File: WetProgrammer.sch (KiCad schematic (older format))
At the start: 31 parts

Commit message: Added power flaggs to supress ERC errors
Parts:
- removed JP?: Jumper_3_Open, symbol Jumper:Jumper_3_Open
- added JP4: SolderJumper_3_Open, symbol Jumper:SolderJumper_3_Open
- JP1: renamed from JP?; symbol tmc:SolderJumper_3_Bridged12 -> WetProgrammer-rescue:SolderJumper_3_Bridged12-tmc
- JP5: renamed from JP?; symbol Jumper:Jumper_2_Open -> Jumper:SolderJumper_2_Open
- U1: renamed from U?; symbol tmc:ATmega32U4-AU -> WetProgrammer-rescue:ATmega32U4-AU-tmc
- Y1: renamed from Y?; symbol tmc:Crystal -> WetProgrammer-rescue:Crystal-tmc
- gave numbers to parts that had none: 24
- renumbered JDUT to JDUT1, JPROG to JPROG1
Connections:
- wire segments 113 -> 120

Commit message: Inital Layout
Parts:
- removed JP4: SolderJumper_3_Open, symbol Jumper:SolderJumper_3_Open
- added SW1: SW_SPDT, tmc:388Switch, symbol Switch:SW_SPDT
- added TP3: TestPoint, TestPoint:TestPoint_Pad_D1.5mm, symbol Connector:TestPoint
- C7, C8: footprint (none) -> Capacitor_SMD:C_0805_2012Metric
- F1: footprint (none) -> Fuse:Fuse_0805_2012Metric_Castellated
- J1: footprint tmc:usbMicro -> 388:usbMicro
- JP1: footprint Jumper:SolderJumper-3_P1.3mm_Bridged12_Pad1.0x1.5mm -> Jumper:SolderJumper-2_P1.3mm_Bridged_Pad1.0x1.5mm; symbol WetProgrammer-rescue:SolderJumper_3_Bridged12-tmc -> Jumper:SolderJumper_2_Bridged
- JP4: renamed from JP5; footprint (none) -> Connector_PinHeader_2.54mm:PinHeader_1x02_P2.54mm_Vertical; symbol Jumper:SolderJumper_2_Open -> Jumper:Jumper_2_Open
- JPROG1: footprint (none) -> Connector_PinHeader_1.27mm:PinHeader_2x05_P1.27mm_Vertical
- TP2: renamed from TP1; footprint TestPoint:TestPoint_Bridge_Pitch2.0mm_Drill0.7mm -> TestPoint:TestPoint_Pad_D1.5mm
- U2: footprint (none) -> Package_TO_SOT_SMD:SOT-223-3_TabPin2
- renumbered C2 to C1, C3 to C2, C1 to C3, JDUT1 to J2
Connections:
- wire segments 120 -> 124
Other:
- moved on the sheet: C3

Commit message: Changes as requested by Ben
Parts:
- removed JP4: Jumper_2_Open, Connector_PinHeader_2.54mm:PinHeader_1x02_P2.54mm_Vertical, symbol Jumper:Jumper_2_Open
- added FID1, FID2: Fiducial, Fiducial:Fiducial_1mm_Mask2mm, symbol Mechanical:Fiducial
- added H1, H2: MountingHole, MountingHole:MountingHole_3.2mm_M3, symbol Mechanical:MountingHole
- added J3: Conn_01x03_Male, Connector_PinHeader_2.54mm:PinHeader_1x03_P2.54mm_Vertical, symbol Connector:Conn_01x03_Male
- added R10, R11: 330, Resistor_SMD:R_0805_2012Metric, symbol Device:R
- added SW2: SW_SPDT, tmc:388Switch, symbol Switch:SW_SPDT
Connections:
- net GND: now also J3.3 (Pin_3)
- net VCC: now also SW2.1 (A)
- net VProg: now also SW2.2 (B)
- net at U1.20 (PD2): now also R10.2
- net at U1.21 (PD3): now also R11.2
- new net RXI: J3.2 (Pin_2), R11.1
- new net TXO: J3.1 (Pin_1), R10.1
- no-connect marks 16 -> 15
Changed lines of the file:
@@
 NoConn ~ 3400 2700
 NoConn ~ 3400 2800
-NoConn ~ 3400 2900
-NoConn ~ 3400 3000
 NoConn ~ 3400 3200
 NoConn ~ 3400 3300
@@
 P 3950 3550
 F 0 "#PWR013" H 3950 3400 50  0001 C CNN
-F 1 "VCC" H 3965 3723 50  0000 C CNN
+F 1 "VCC" H 3950 3700 50  0000 C CNN
 F 2 "" H 3950 3550 50  0001 C CNN
 F 3 "" H 3950 3550 50  0001 C CNN
@@
 	9500 1550 9500 1500
 $Comp
-L Jumper:Jumper_2_Open JP4
-U 1 1 6137D06D
-P 9200 1900
-F 0 "JP4" H 9200 1800 50  0000 C CNN
-F 1 "Jumper_2_Open" H 9200 1766 50  0001 C CNN
-F 2 "Connector_PinHeader_2.54mm:PinHeader_1x02_P2.54mm_Vertical" H 9200 1900 50  0001 C CNN
-F 3 "~" H 9200 1900 50  0001 C CNN
-	1    9200 1900
-	-1   0    0    1
-$EndComp
-$Comp
 L power:VCC #PWR021
 U 1 1 6137EE6D
-P 8950 1850
-F 0 "#PWR021" H 8950 1700 50  0001 C CNN
-F 1 "VCC" H 8965 2023 50  0000 C CNN
-F 2 "" H 8950 1850 50  0001 C CNN
-F 3 "" H 8950 1850 50  0001 C CNN
-	1    8950 1850
-	1    0    0    -1
-$EndComp
-Wire Wire Line
-	8950 1850 8950 1900
-Wire Wire Line
-	8950 1900 9000 1900
-Wire Wire Line
-	9400 1900 9650 1900
-Text Label 9650 1900 2    50   ~ 0
+P 8950 1900
+F 0 "#PWR021" H 8950 1750 50  0001 C CNN
+F 1 "VCC" H 8965 2073 50  0000 C CNN
+F 2 "" H 8950 1900 50  0001 C CNN
+F 3 "" H 8950 1900 50  0001 C CNN
+	1    8950 1900
+	1    0    0    -1
+$EndComp
+Wire Wire Line
+	8950 1900 8950 1950
+Wire Wire Line
+	8950 1950 9000 1950
+Wire Wire Line
+	9400 2050 9650 2050
+Text Label 9650 2050 2    50   ~ 0
 VProg
 Wire Wire Line
@@
 Text Notes 8900 700  0    50   ~ 0
 Voltage Select Jumper
-Text Notes 8950 2150 0    50   ~ 0
+Text Notes 8950 2400 0    50   ~ 0
 Programer Provides\nPower Select
 Text Notes 8050 850  0    50   ~ 0
@@
 Wire Wire Line
 	3800 2200 3800 2050
+$Comp
+L Mechanical:Fiducial FID2
+U 1 1 61492763
+P 650 7400
+F 0 "FID2" H 735 7446 50  0000 L CNN
+F 1 "Fiducial" H 735 7355 50  0000 L CNN
+F 2 "Fiducial:Fiducial_1mm_Mask2mm" H 650 7400 50  0001 C CNN
+F 3 "~" H 650 7400 50  0001 C CNN
+	1    650  7400
+	1    0    0    -1
+$EndComp
+$Comp
+L Mechanical:Fiducial FID1
+U 1 1 61492FAD
+P 650 7200
+F 0 "FID1" H 735 7246 50  0000 L CNN
+F 1 "Fiducial" H 735 7155 50  0000 L CNN
+F 2 "Fiducial:Fiducial_1mm_Mask2mm" H 650 7200 50  0001 C CNN
+F 3 "~" H 650 7200 50  0001 C CNN
+	1    650  7200
+	1    0    0    -1
+$EndComp
+$Comp
+L Mechanical:MountingHole H1
+U 1 1 61497033
+P 650 7600
+F 0 "H1" H 750 7646 50  0000 L CNN
+F 1 "MountingHole" H 750 7555 50  0000 L CNN
+F 2 "MountingHole:MountingHole_3.2mm_M3" H 650 7600 50  0001 C CNN
+F 3 "~" H 650 7600 50  0001 C CNN
+	1    650  7600
+	1    0    0    -1
+$EndComp
+$Comp
+L Mechanical:MountingHole H2
+U 1 1 6149BCA9
+P 650 7800
+F 0 "H2" H 750 7846 50  0000 L CNN
+F 1 "MountingHole" H 750 7755 50  0000 L CNN
+F 2 "MountingHole:MountingHole_3.2mm_M3" H 650 7800 50  0001 C CNN
+F 3 "~" H 650 7800 50  0001 C CNN
+	1    650  7800
+	1    0    0    -1
+$EndComp
+$Comp
+L Switch:SW_SPDT SW2
+U 1 1 614A9941
+P 9200 2050
+F 0 "SW2" H 9100 2150 50  0000 R CNN
+F 1 "SW_SPDT" V 9245 1862 50  0001 R CNN
+F 2 "tmc:388Switch" H 9200 2050 50  0001 C CNN
+F 3 "~" H 9200 2050 50  0001 C CNN
+	1    9200 2050
+	-1   0    0    -1
+$EndComp
+NoConn ~ 9000 2150
+$Comp
+L Device:R R?
+U 1 1 614D3179
+P 3600 2900
+AR Path="/612E47B1/614D3179" Ref="R?"  Part="1"
+AR Path="/614D3179" Ref="R10"  Part="1"
+F 0 "R10" V 3550 3100 50  0000 C CNN
+F 1 "330" V 3600 2900 50  0000 C CNN
+F 2 "Resistor_SMD:R_0805_2012Metric" V 3530 2900 50  0001 C CNN
+F 3 "~" H 3600 2900 50  0001 C CNN
+	1    3600 2900
+	0    1    1    0
+$EndComp
+Wire Wire Line
+	3450 2900 3400 2900
+$Comp
+L Device:R R?
+U 1 1 614D6E84
+P 3600 3000
+AR Path="/612E47B1/614D6E84" Ref="R?"  Part="1"
+AR Path="/614D6E84" Ref="R11"  Part="1"
+F 0 "R11" V 3550 3200 50  0000 C CNN
+F 1 "330" V 3600 3000 50  0000 C CNN
+F 2 "Resistor_SMD:R_0805_2012Metric" V 3530 3000 50  0001 C CNN
+F 3 "~" H 3600 3000 50  0001 C CNN
+	1    3600 3000
+	0    1    1    0
+$EndComp
+Wire Wire Line
+	3450 3000 3400 3000
+Text Label 4050 3000 2    50   ~ 0
+RXI
+Text Label 4050 2900 2    50   ~ 0
+TXO
+$Comp
+L Connector:Conn_01x03_Male J3
+U 1 1 614ECA92
+P 4300 3000
+F 0 "J3" H 4272 2978 50  0000 R CNN
+F 1 "Conn_01x03_Male" H 4272 2933 50  0001 R CNN
+F 2 "Connector_PinHeader_2.54mm:PinHeader_1x03_P2.54mm_Vertical" H 4300 3000 50  0001 C CNN
+F 3 "~" H 4300 3000 50  0001 C CNN
+	1    4300 3000
+	-1   0    0    -1
+$EndComp
+Wire Wire Line
+	3750 2900 4100 2900
+Wire Wire Line
+	3750 3000 4100 3000
+$Comp
+L power:GND #PWR?
+U 1 1 614F6BB5
+P 4050 3150
+AR Path="/612E47B1/614F6BB5" Ref="#PWR?"  Part="1"
+AR Path="/614F6BB5" Ref="#PWR0101"  Part="1"
+F 0 "#PWR0101" H 4050 2900 50  0001 C CNN
+F 1 "GND" H 4050 3000 50  0000 C CNN
+F 2 "" H 4050 3150 50  0001 C CNN
+F 3 "" H 4050 3150 50  0001 C CNN
+	1    4050 3150
+	1    0    0    -1
+$EndComp
+Wire Wire Line
+	4050 3150 4050 3100
+Wire Wire Line
+	4050 3100 4100 3100
 $EndSCHEMATC

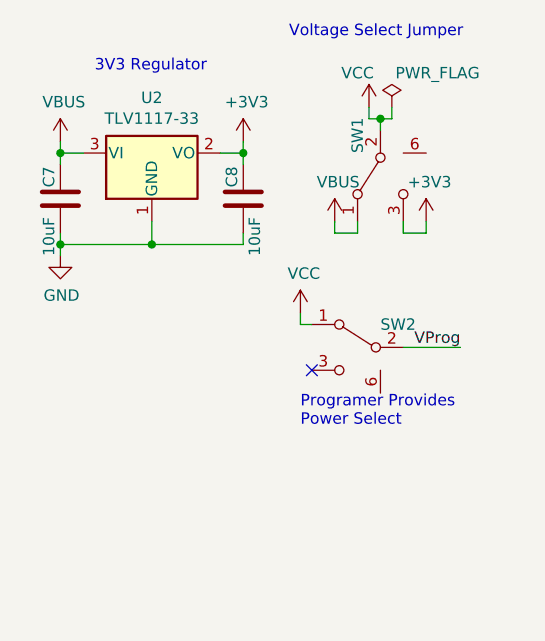
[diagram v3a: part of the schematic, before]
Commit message: Connected swtich sheilding to gnd
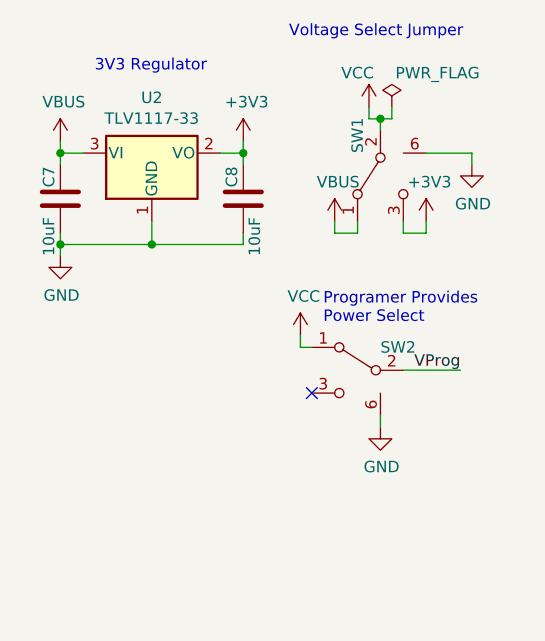
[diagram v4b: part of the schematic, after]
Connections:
- net GND: now also SW1.6 (sheild), SW2.6 (sheild)
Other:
- moved on the sheet: SW2
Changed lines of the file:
@@
 Connection ~ 8300 1600
-$Comp
-L power:VBUS #PWR?
-U 1 1 6136D7E0
-P 9100 1500
-AR Path="/612E47B1/6136D7E0" Ref="#PWR?"  Part="1"
-AR Path="/6136D7E0" Ref="#PWR022"  Part="1"
-F 0 "#PWR022" H 9100 1350 50  0001 C CNN
-F 1 "VBUS" H 9115 1673 50  0000 C CNN
-F 2 "" H 9100 1500 50  0001 C CNN
-F 3 "" H 9100 1500 50  0001 C CNN
-	1    9100 1500
-	1    0    0    -1
-$EndComp
-$Comp
-L power:+3V3 #PWR?
-U 1 1 613709A8
-P 9500 1500
-AR Path="/612E47B1/613709A8" Ref="#PWR?"  Part="1"
-AR Path="/613709A8" Ref="#PWR024"  Part="1"
-F 0 "#PWR024" H 9500 1350 50  0001 C CNN
-F 1 "+3V3" H 9515 1673 50  0000 C CNN
-F 2 "" H 9500 1500 50  0001 C CNN
-F 3 "" H 9500 1500 50  0001 C CNN
-	1    9500 1500
-	1    0    0    -1
-$EndComp
-$Comp
-L power:VCC #PWR023
-U 1 1 61370E3F
-P 9250 1000
-F 0 "#PWR023" H 9250 850 50  0001 C CNN
-F 1 "VCC" H 9200 1150 50  0000 C CNN
-F 2 "" H 9250 1000 50  0001 C CNN
-F 3 "" H 9250 1000 50  0001 C CNN
-	1    9250 1000
-	1    0    0    -1
-$EndComp
-Wire Wire Line
-	9100 1550 9100 1500
-Wire Wire Line
-	9500 1550 9500 1500
 $Comp
 L power:VCC #PWR021
 U 1 1 6137EE6D
-P 8950 1900
-F 0 "#PWR021" H 8950 1750 50  0001 C CNN
-F 1 "VCC" H 8965 2073 50  0000 C CNN
-F 2 "" H 8950 1900 50  0001 C CNN
-F 3 "" H 8950 1900 50  0001 C CNN
-	1    8950 1900
-	1    0    0    -1
-$EndComp
-Wire Wire Line
-	8950 1900 8950 1950
-Wire Wire Line
-	8950 1950 9000 1950
-Wire Wire Line
-	9400 2050 9650 2050
-Text Label 9650 2050 2    50   ~ 0
+P 8950 2000
+F 0 "#PWR021" H 8950 1850 50  0001 C CNN
+F 1 "VCC" H 8965 2173 50  0000 C CNN
+F 2 "" H 8950 2000 50  0001 C CNN
+F 3 "" H 8950 2000 50  0001 C CNN
+	1    8950 2000
+	1    0    0    -1
+$EndComp
+Wire Wire Line
+	8950 2000 8950 2050
+Wire Wire Line
+	8950 2050 9000 2050
+Wire Wire Line
+	9400 2150 9650 2150
+Text Label 9650 2150 2    50   ~ 0
 VProg
 Wire Wire Line
@@
 Text Notes 8900 700  0    50   ~ 0
 Voltage Select Jumper
-Text Notes 8950 2400 0    50   ~ 0
+Text Notes 9050 1950 0    50   ~ 0
 Programer Provides\nPower Select
 Text Notes 8050 850  0    50   ~ 0
@@
 	1400 2650 1400 2600
 Connection ~ 1400 2650
-$Comp
-L power:PWR_FLAG #FLG02
-U 1 1 61448067
-P 9350 1000
-F 0 "#FLG02" H 9350 1075 50  0001 C CNN
-F 1 "PWR_FLAG" H 9550 1150 50  0000 C CNN
-F 2 "" H 9350 1000 50  0001 C CNN
-F 3 "~" H 9350 1000 50  0001 C CNN
-	1    9350 1000
-	1    0    0    -1
-$EndComp
-Wire Wire Line
-	9350 1000 9350 1050
-Wire Wire Line
-	9350 1050 9300 1050
-Wire Wire Line
-	9250 1050 9250 1000
-Wire Wire Line
-	9300 1100 9300 1050
-Connection ~ 9300 1050
-Wire Wire Line
-	9300 1050 9250 1050
 $Comp
 L Jumper:SolderJumper_2_Bridged JP?
@@
 Wire Wire Line
 	3800 2050 3800 2000
-$Comp
-L Switch:SW_SPDT SW1
-U 1 1 61486C4E
-P 9300 1300
-F 0 "SW1" H 9200 1400 50  0000 R CNN
-F 1 "SW_SPDT" V 9345 1112 50  0001 R CNN
-F 2 "tmc:388Switch" H 9300 1300 50  0001 C CNN
-F 3 "~" H 9300 1300 50  0001 C CNN
-	1    9300 1300
-	0    -1   1    0
-$EndComp
-Wire Wire Line
-	9200 1550 9200 1500
 Wire Wire Line
 	9100 1550 9200 1550
-Wire Wire Line
-	9400 1550 9400 1500
 Wire Wire Line
 	9400 1550 9500 1550
@@
 L Switch:SW_SPDT SW2
 U 1 1 614A9941
-P 9200 2050
-F 0 "SW2" H 9100 2150 50  0000 R CNN
-F 1 "SW_SPDT" V 9245 1862 50  0001 R CNN
-F 2 "tmc:388Switch" H 9200 2050 50  0001 C CNN
-F 3 "~" H 9200 2050 50  0001 C CNN
-	1    9200 2050
+P 9200 2150
+F 0 "SW2" H 9100 2250 50  0000 R CNN
+F 1 "SW_SPDT" V 9245 1962 50  0001 R CNN
+F 2 "tmc:388Switch" H 9200 2150 50  0001 C CNN
+F 3 "~" H 9200 2150 50  0001 C CNN
+	1    9200 2150
 	-1   0    0    -1
 $EndComp
-NoConn ~ 9000 2150
+NoConn ~ 9000 2250
 $Comp
 L Device:R R?
@@
 Wire Wire Line
 	4050 3100 4100 3100
+$Comp
+L power:GND #PWR?
+U 1 1 614B5DDC
+P 9700 1250
+F 0 "#PWR?" H 9700 1000 50  0001 C CNN
+F 1 "GND" H 9705 1077 50  0000 C CNN
+F 2 "" H 9700 1250 50  0001 C CNN
+F 3 "" H 9700 1250 50  0001 C CNN
+	1    9700 1250
+	1    0    0    -1
+$EndComp
+Wire Wire Line
+	9400 1550 9400 1500
+Wire Wire Line
+	9200 1550 9200 1500
+$Comp
+L Switch:SW_SPDT SW1
+U 1 1 61486C4E
+P 9300 1300
+F 0 "SW1" H 9200 1400 50  0000 R CNN
+F 1 "SW_SPDT" V 9345 1112 50  0001 R CNN
+F 2 "tmc:388Switch" H 9300 1300 50  0001 C CNN
+F 3 "~" H 9300 1300 50  0001 C CNN
+	1    9300 1300
+	0    -1   1    0
+$EndComp
+Wire Wire Line
+	9300 1050 9250 1050
+Connection ~ 9300 1050
+Wire Wire Line
+	9300 1100 9300 1050
+Wire Wire Line
+	9250 1050 9250 1000
+Wire Wire Line
+	9350 1050 9300 1050
+Wire Wire Line
+	9350 1000 9350 1050
+$Comp
+L power:PWR_FLAG #FLG02
+U 1 1 61448067
+P 9350 1000
+F 0 "#FLG02" H 9350 1075 50  0001 C CNN
+F 1 "PWR_FLAG" H 9550 1150 50  0000 C CNN
+F 2 "" H 9350 1000 50  0001 C CNN
+F 3 "~" H 9350 1000 50  0001 C CNN
+	1    9350 1000
+	1    0    0    -1
+$EndComp
+Wire Wire Line
+	9500 1550 9500 1500
+Wire Wire Line
+	9100 1550 9100 1500
+$Comp
+L power:VCC #PWR023
+U 1 1 61370E3F
+P 9250 1000
+F 0 "#PWR023" H 9250 850 50  0001 C CNN
+F 1 "VCC" H 9200 1150 50  0000 C CNN
+F 2 "" H 9250 1000 50  0001 C CNN
+F 3 "" H 9250 1000 50  0001 C CNN
+	1    9250 1000
+	1    0    0    -1
+$EndComp
+$Comp
+L power:+3V3 #PWR?
+U 1 1 613709A8
+P 9500 1500
+AR Path="/612E47B1/613709A8" Ref="#PWR?"  Part="1"
+AR Path="/613709A8" Ref="#PWR024"  Part="1"
+F 0 "#PWR024" H 9500 1350 50  0001 C CNN
+F 1 "+3V3" H 9515 1673 50  0000 C CNN
+F 2 "" H 9500 1500 50  0001 C CNN
+F 3 "" H 9500 1500 50  0001 C CNN
+	1    9500 1500
+	1    0    0    -1
+$EndComp
+$Comp
+L power:VBUS #PWR?
+U 1 1 6136D7E0
+P 9100 1500
+AR Path="/612E47B1/6136D7E0" Ref="#PWR?"  Part="1"
+AR Path="/6136D7E0" Ref="#PWR022"  Part="1"
+F 0 "#PWR022" H 9100 1350 50  0001 C CNN
+F 1 "VBUS" H 9115 1673 50  0000 C CNN
+F 2 "" H 9100 1500 50  0001 C CNN
+F 3 "" H 9100 1500 50  0001 C CNN
+	1    9100 1500
+	1    0    0    -1
+$EndComp
+Wire Wire Line
+	9500 1200 9700 1200
+Wire Wire Line
+	9700 1200 9700 1250
+$Comp
+L power:GND #PWR?
+U 1 1 614BD717
+P 9300 2400
+F 0 "#PWR?" H 9300 2150 50  0001 C CNN
+F 1 "GND" H 9305 2227 50  0000 C CNN
+F 2 "" H 9300 2400 50  0001 C CNN
+F 3 "" H 9300 2400 50  0001 C CNN
+	1    9300 2400
+	1    0    0    -1
+$EndComp
+Wire Wire Line
+	9300 2400 9300 2350
 $EndSCHEMATC

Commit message: Changed programmer port to JTAG
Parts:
- removed JP1: SolderJumper_3_Bridged12, Jumper:SolderJumper-2_P1.3mm_Bridged_Pad1.0x1.5mm, symbol Jumper:SolderJumper_2_Bridged
- added C9: 100nF, Capacitor_SMD:C_0805_2012Metric, symbol Device:C
- JPROG1: symbol Connector:AVR-ISP-10 -> Connector:AVR-JTAG-10
- Y1: footprint Crystal:Crystal_SMD_HC49-SD -> Crystal:Crystal_SMD_3225-4Pin_3.2x2.5mm; symbol WetProgrammer-rescue:Crystal-tmc -> Device:Crystal_GND24_Small
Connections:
- net GND: now also JPROG1.2 (GND), Y1.2, Y1.4, C9.1; no longer JPROG1.4 (GND), JPROG1.6 (GND), JPROG1.8 (GND)
- net MISO: no longer JPROG1.9 (MISO)
- net MOSI: no longer JPROG1.1 (MOSI)
- net RstP: now also JPROG1.6 (~SRST), C9.2; no longer JPROG1.5 (~RST)
- net SCK: no longer JPROG1.7 (SCK)
- net VCC: now also C3.2, JPROG1.4 (VREF), SW2.2 (B), U1.42 (AREF); no longer JPROG1.2 (VCC), SW2.1 (A)
- net VProg: now also SW2.3 (C); no longer SW2.2 (B)
- net Xtal1: now reaches C1.2, U1.17 (XTAL1), Y1.1
- net Xtal2: now reaches C2.2, U1.16 (XTAL2)
- net Xtal2: now also Y1.3; no longer Y1.2
- net UD+: now reaches R1.1, U1.4 (D+)
- net D+: now reaches J1.3 (D+), R1.2
- net UD-: now reaches R2.1, U1.3 (D-)
- net D-: now reaches J1.2 (D-), R2.2
- net TDI: now reaches U1.36 (PF7)
- net TDI: now also JPROG1.9 (TDI)
- net TDO: now reaches U1.37 (PF6)
- net TDO: now also JPROG1.3 (TDO)
- net TMS: now reaches U1.38 (PF5)
- net TMS: now also JPROG1.5 (TMS)
- net TCK: now reaches U1.39 (PF4)
- net TCK: now also JPROG1.1 (TCK)
- no-connect marks 15 -> 13
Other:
- moved on the sheet: C1, C2, J2, JP2, R3, R5, R7, R8, R9
